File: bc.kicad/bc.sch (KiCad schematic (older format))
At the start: 19 parts, among them J1 Pin_Header_01x33_Male, J2 Capacitive Keyboard

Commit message: Experiment with keyboard backlighting
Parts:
- removed D1: LED_C1, bc:side_led, symbol Device:LED_Small
- removed D10: LED_A1_T, bc:side_led, symbol Device:LED_Small
- removed D11: LED_A1_B, bc:side_led, symbol Device:LED_Small
- removed D12: LED_A#1, bc:side_led, symbol Device:LED_Small
- removed D13: LED_B1_T, bc:side_led, symbol Device:LED_Small
- removed D14: LED_B1_B, bc:side_led, symbol Device:LED_Small
- removed D15: LED_C2_T, bc:side_led, symbol Device:LED_Small
- removed D16: LED_C2_B, bc:side_led, symbol Device:LED_Small
- removed D2: LED_C#1, bc:side_led, symbol Device:LED_Small
- removed D3: LED_D1, bc:side_led, symbol Device:LED_Small
- removed D4: LED_D#1, bc:side_led, symbol Device:LED_Small
- removed D5: LED_E1, bc:side_led, symbol Device:LED_Small
- removed D6: LED_F1, bc:side_led, symbol Device:LED_Small
- removed D7: LED_F#1, bc:side_led, symbol Device:LED_Small
- removed D8: LED_G1, bc:side_led, symbol Device:LED_Small
- removed D9: LED_G#1, bc:side_led, symbol Device:LED_Small
- removed J1: Pin_Header_01x33_Male, Connector_PinHeader_2.54mm:PinHeader_1x33_P2.54mm_Vertical_SMD_Pin1Left, symbol Connector:Conn_01x33_Male
- added BT?: CR2016, Battery:BatteryHolder_Keystone_3002_1x2032, symbol Device:Battery_Cell
- added C? (x6): 500nF, symbol Device:C
- added D? (x4): D_Schottky, symbol Device:D_Schottky
- added D? (x21): LED, symbol Device:LED
- added J?: Edge Connector, symbol Connector:Conn_01x08_Male
- added U?: STM32L052C8Tx, Package_QFP:LQFP-48_7x7mm_P0.5mm, symbol MCU_ST_STM32L0:STM32L052C8Tx
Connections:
- net labels added: BOOT0, DAC_OUT, GND, KEY_01_C1, KEY_02_C#1, KEY_03_D1, KEY_04_D#1, KEY_05_E1, KEY_06_F1, KEY_07_F#1, KEY_08_G1, KEY_09_G#1, KEY_10_A1, KEY_11_A#1, KEY_12_B1, KEY_13_C2, KEY_SAMP_C1, KEY_SAMP_C2, KEY_SAMP_C3, KEY_SAMP_C4, KEY_SAMP_C5, LED_C0, LED_C2, LED_C3, LED_R0, LED_R1, LED_R2, LED_R3, NRST, SWCLK, SWDIO, USART_RX, USART_TX, VDD
- net labels removed: ACT_SHLD, CAP_A#1, CAP_A1, CAP_B1, CAP_C#1, CAP_C1, CAP_C2, CAP_D#1, CAP_D1, CAP_E1, CAP_F#1, CAP_F1, CAP_G#1, CAP_G1, GNDD, LED_A#1, LED_A1_B, LED_A1_T, LED_B1_B, LED_B1_T, LED_C#1, LED_C2_B, LED_C2_T, LED_D#1, LED_D1, LED_E1, LED_F#1, LED_F1, LED_G#1, LED_G1, LED_GND, SPEAKER+, SPEAKER-
- wire segments 72 -> 146
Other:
- moved on the sheet: J2

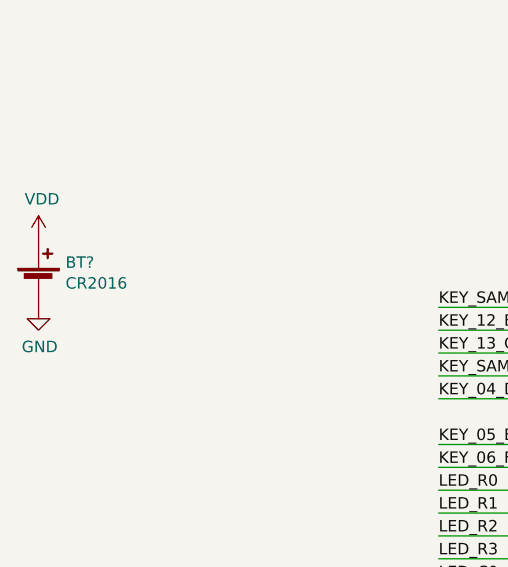
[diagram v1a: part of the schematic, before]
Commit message: Switch from CR2016 to CR2032
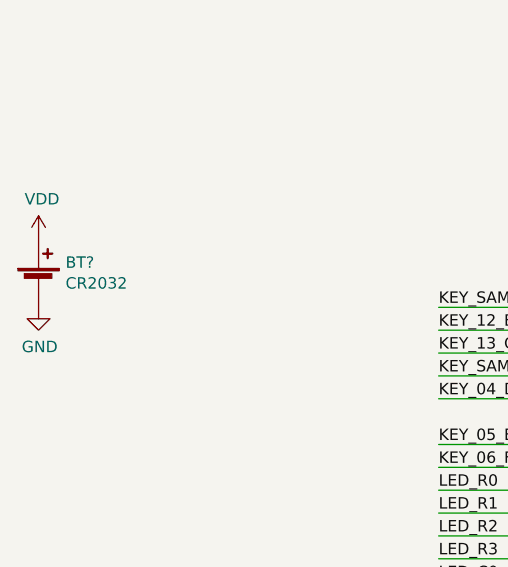
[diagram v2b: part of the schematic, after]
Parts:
- BT?: value CR2016 -> CR2032
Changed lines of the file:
@@
 P 1200 5450
 F 0 "BT?" H 1318 5546 50  0000 L CNN
-F 1 "CR2016" H 1318 5455 50  0000 L CNN
+F 1 "CR2032" H 1318 5455 50  0000 L CNN
 F 2 "Battery:BatteryHolder_Keystone_3002_1x2032" V 1200 5510 50  0001 C CNN
 F 3 "~" V 1200 5510 50  0001 C CNN

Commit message: Verify touch sensing design
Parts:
- removed J2: Capacitive Keyboard, bc:keyboard, symbol Connector:Conn_01x13_Female
- removed LS1: Speaker, bc:wire_pad_3x5mm_x2, symbol Device:Speaker
- added C? (x8): 500nF, symbol Device:C
- added C? (x12): 100nF, symbol Device:C
- added C? (x2): Capacitive_Keyboard, symbol bc:Capacitive_Keyboard
- added D? (x5): D_Schottky, symbol Device:D_Schottky
- added D? (x8): LED, symbol Device:LED
- added LS?: Transducer, symbol Device:Speaker_Crystal
- added Q?: PMV48XP, symbol Device:Q_PMOS_GSD
- added R? (x20): 10K, symbol Device:R
- added SW?: SW_Push, symbol Switch:SW_Push
- U?: symbol MCU_ST_STM32L0:STM32L052C8Tx -> bc:STM32L052C8Tx
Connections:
- net BOOT0: now also U?.44 (BOOT0), R?.2
- net GND: now also C?.1, C?.1, C?.1, C?.1, C?.1, C?.1, C?.1, C?.2, C?.2, C?.2, LS?.2, Q?.1 (G), R?.1, R?.1
- net KEY_01_C1: now also R?.1
- net KEY_02_C#1: now also R?.1
- net KEY_03_D1: now also R?.1
- net KEY_04_D#1: now also U?.16 (PA6), R?.1; no longer U?.40 (PB4)
- net KEY_05_E1: now also U?.17 (PA7), R?.1; no longer U?.42 (PB6)
- net KEY_06_F1: now also U?.19 (PB1), R?.1; no longer U?.43 (PB7)
- net KEY_07_F#1: now also U?.20 (PB2), R?.1; no longer U?.31 (PA10)
- net KEY_08_G1: now also U?.31 (PA10), R?.1; no longer U?.32 (PA11)
- net KEY_09_G#1: now also U?.32 (PA11), R?.1, R?.1; no longer U?.33 (PA12)
- net KEY_10_A1: now also U?.33 (PA12), R?.1, R?.1; no longer U?.16 (PA6)
- net KEY_11_A#1: now also U?.40 (PB4), R?.1, R?.1; no longer U?.17 (PA7)
- net KEY_12_B1: now also U?.42 (PB6), R?.1, R?.1; no longer U?.19 (PB1)
- net KEY_13_C2: now also U?.43 (PB7), R?.1, R?.1; no longer U?.20 (PB2)
- net KEY_SAMP_C1: now also C?.2
- net KEY_SAMP_C2: now also U?.15 (PA5), C?.2; no longer U?.39 (PB3)
- net KEY_SAMP_C3: now also U?.18 (PB0), C?.2; no longer U?.30 (PA9)
- net KEY_SAMP_C4: now also U?.30 (PA9), C?.2, C?.2; no longer U?.15 (PA5)
- net KEY_SAMP_C5: now also U?.39 (PB3), C?.2, C?.2; no longer U?.18 (PB0)
- net LED_C0: now also C?.1
- net LED_C1: now also D?.1 (K), D?.1 (K), D?.1 (K), D?.1 (K), D?.1 (K), D?.1 (K), D?.1 (K), D?.1 (K)
- net LED_R0: now also C?.1, C?.1
- net LED_R1: now also C?.1, C?.1
- net LED_R2: now also C?.1, C?.1
- net LED_R3: now also C?.1
- net NRST: now also U?.7 (NRST), C?.1
- net SWCLK: now also U?.37 (PA14)
- net SWDIO: now also U?.34 (PA13)
- net VDD: now also U?.1 (VDD), C?.1, C?.1, C?.1, C?.1, D?.2 (A), D?.2 (A), D?.2 (A), D?.2 (A), D?.2 (A), Q?.2 (S), SW?.1; no longer BT?.1 (+)
- net WKUP_MODE: now reaches U?.2 (PC13)
- net WKUP_MODE: now also R?.2, SW?.2
- net TRANSDUCER: now reaches U?.41 (PB5)
- net TRANSDUCER: now also LS?.1
- new net: BT?.1 (+), Q?.3 (D)
- new net: C?.2, C?.2, D?.1 (K), D?.2 (A), D?.2 (A) (x3)
- new net: C?.2, D?.1 (K), D?.2 (A) (x2)
- new net: C?.10 (10_A1), R?.2 (x2)
- new net: C?.11 (11_A#1), R?.2 (x2)
- new net: C?.12 (12_B1), R?.2 (x2)
- new net: C?.13 (13_C2), R?.2 (x2)
- new net: C?.9 (09_G#1), R?.2 (x2)
- new net: C?.1 (01_C1), R?.2
- new net: C?.2 (02_C#1), R?.2
- new net: C?.3 (03_D1), R?.2
- new net: C?.4 (04_D#1), R?.2
- new net: C?.5 (05_E1), R?.2
- new net: C?.6 (06_F1), R?.2
- new net: C?.7 (07_F#1), R?.2
- new net: C?.8 (08_G1), R?.2
- no-connect marks 0 -> 6
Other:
- note added: "1"
- note added: "2"
- note added: "3"
- note added: "4"
- note added: "5"
- note added: "CAP1"
- note added: "CAP2"
- note added: "CAP3"
- note added: "CAP4"
- note added: "CAP5"
- note added: "KEY01"
- note added: "KEY02"
- note added: "KEY03"
- note added: "KEY04"
- note added: "KEY05"
- note added: "KEY06"
- note added: "KEY07"
- note added: "KEY08"
- note added: "KEY09"
- note added: "KEY10"
- note added: "KEY11"
- note added: "KEY12"
- note added: "KEY13"
- note added: "PA11"
- note added: "PA12"
- note added: "PA9"
- note added: "PB10"
- note added: "PB11"
- note added: "PB12"
- note added: "PB13"
- note added: "PB3"
- note added: "PB4"
- note added: "PB6"
- note added: "PB7"
- note added: "PB8"
- note added: "PB9"
- note added: "TSC groups\n\n1: PA0-PA3\n2: PA5-PA7\n3: PB0-PB2\n4: PA9-PA12\n5: PB3, PB4, PB6, PB7"
- moved on the sheet: BT?, C?, D?, J?, U?

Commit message: Validate LED control circuit
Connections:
- net labels added: LED_R0_CLK, LED_R0_PWR, LED_R1_CLK, LED_R1_PWR, LED_R2_CLK, LED_R2_PWR, LED_R3_CLK, LED_R3_PWR
- net labels removed: DAC_OUT, LED_R0, LED_R1, LED_R2, LED_R3
- wire segments 242 -> 256
- no-connect marks 6 -> 3
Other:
- note added: "PA4"
- note added: "PA5"
- note added: "PA6"
- note added: "PA7"
- note added: "PA8"
- note removed: "PB13"
- moved on the sheet: C?, D?, R?

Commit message: Connect VDD to ADC
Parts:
- removed C? (x8): 500nF, symbol Device:C
- removed C?: Capacitive_Keyboard, symbol bc:Capacitive_Keyboard
- removed C? (x2): 100nF, symbol Device:C
- removed D? (x5): D_Schottky, symbol Device:D_Schottky
- removed D? (x8): LED, symbol Device:LED
- removed R? (x5): 10K, symbol Device:R
- added R2: 10K, symbol Device:R
- gave numbers to parts that had none: 63
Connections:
- net labels added: VDD_ADC
- wire segments 256 -> 202
- no-connect marks 3 -> 2
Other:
- note removed: "PA11"
- note removed: "PA12"
- note removed: "PA4"
- note removed: "PA5"
- note removed: "PA6"
- note removed: "PA7"
- note removed: "PA8"
- note removed: "PA9"
- note removed: "PB10"
- note removed: "PB11"
- note removed: "PB12"
- note removed: "PB3"
- note removed: "PB4"
- note removed: "PB6"
- note removed: "PB7"
- note removed: "PB8"
- note removed: "PB9"
- moved on the sheet: BT1, C10, C8, Q1

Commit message: Add bypassing to compensate for LED boosters
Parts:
- added C11, C12, C13, C14: 500nF, symbol Device:C
- renumbered C11 to C15, C12 to C16, C13 to C17, C14 to C18, C15 to C19, C16 to C20, C17 to C21
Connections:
- net GND: now also C11.2, C12.2, C13.2, C14.2
- net VDD: now also C11.1, C12.1, C13.1, C14.1
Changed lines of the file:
@@
 $EndComp
 $Comp
-L power:VDD #PWR014
+L power:VDD #PWR022
 U 1 1 5FD47C4E
 P 6100 3500
-F 0 "#PWR014" H 6100 3350 50  0001 C CNN
+F 0 "#PWR022" H 6100 3350 50  0001 C CNN
 F 1 "VDD" H 6115 3673 50  0000 C CNN
 F 2 "" H 6100 3500 50  0001 C CNN
@@
 $EndComp
 $Comp
-L power:GND #PWR015
+L power:GND #PWR023
 U 1 1 5FD4B605
 P 6100 3800
-F 0 "#PWR015" H 6100 3550 50  0001 C CNN
+F 0 "#PWR023" H 6100 3550 50  0001 C CNN
 F 1 "GND" H 6105 3627 50  0000 C CNN
 F 2 "" H 6100 3800 50  0001 C CNN
@@
 	6450 1550 6150 1550
 $Comp
-L power:GND #PWR019
+L power:GND #PWR027
 U 1 1 5FF011C9
 P 6850 1850
-F 0 "#PWR019" H 6850 1600 50  0001 C CNN
+F 0 "#PWR027" H 6850 1600 50  0001 C CNN
 F 1 "GND" H 6855 1677 50  0000 C CNN
 F 2 "" H 6850 1850 50  0001 C CNN
@@
 $EndComp
 $Comp
-L Device:C C11
+L Device:C C15
 U 1 1 5FD8985A
 P 6450 1700
-F 0 "C11" H 6565 1746 50  0000 L CNN
+F 0 "C15" H 6565 1746 50  0000 L CNN
 F 1 "100nF" H 6565 1655 50  0000 L CNN
 F 2 "" H 6488 1550 50  0001 C CNN
@@
 Connection ~ 6450 1550
 $Comp
-L power:GND #PWR017
+L power:GND #PWR025
 U 1 1 5FDD714C
 P 6450 1850
-F 0 "#PWR017" H 6450 1600 50  0001 C CNN
+F 0 "#PWR025" H 6450 1600 50  0001 C CNN
 F 1 "GND" H 6455 1677 50  0000 C CNN
 F 2 "" H 6450 1850 50  0001 C CNN
@@
 $EndComp
 $Comp
-L power:VDD #PWR018
+L power:VDD #PWR026
 U 1 1 5FEFF5F2
 P 6850 750
-F 0 "#PWR018" H 6850 600 50  0001 C CNN
+F 0 "#PWR026" H 6850 600 50  0001 C CNN
 F 1 "VDD" H 6865 923 50  0000 C CNN
 F 2 "" H 6850 750 50  0001 C CNN
@@
 NoConn ~ 2400 2100
 $Comp
-L power:GND #PWR016
+L power:GND #PWR024
 U 1 1 5FED77A2
 P 6250 650
-F 0 "#PWR016" H 6250 400 50  0001 C CNN
+F 0 "#PWR024" H 6250 400 50  0001 C CNN
 F 1 "GND" H 6255 477 50  0000 C CNN
 F 2 "" H 6250 650 50  0001 C CNN
@@
 CAP5
 $Comp
-L Device:C C12
+L Device:C C16
 U 1 1 602A0CFC
 P 8450 850
-F 0 "C12" V 8198 850 50  0000 C CNN
+F 0 "C16" V 8198 850 50  0000 C CNN
 F 1 "100nF" V 8289 850 50  0000 C CNN
 F 2 "" H 8488 700 50  0001 C CNN
@@
 	7750 850  8300 850
 $Comp
-L power:GND #PWR020
+L power:GND #PWR028
 U 1 1 602CDE2E
 P 8700 850
-F 0 "#PWR020" H 8700 600 50  0001 C CNN
+F 0 "#PWR028" H 8700 600 50  0001 C CNN
 F 1 "GND" H 8705 677 50  0000 C CNN
 F 2 "" H 8700 850 50  0001 C CNN
@@
 $EndComp
 $Comp
-L Device:C C13
+L Device:C C17
 U 1 1 602E6718
 P 8450 1250
-F 0 "C13" V 8198 1250 50  0000 C CNN
+F 0 "C17" V 8198 1250 50  0000 C CNN
 F 1 "100nF" V 8289 1250 50  0000 C CNN
 F 2 "" H 8488 1100 50  0001 C CNN
@@
 	7750 1250 8300 1250
 $Comp
-L power:GND #PWR021
+L power:GND #PWR029
 U 1 1 602E6720
 P 8700 1250
-F 0 "#PWR021" H 8700 1000 50  0001 C CNN
+F 0 "#PWR029" H 8700 1000 50  0001 C CNN
 F 1 "GND" H 8705 1077 50  0000 C CNN
 F 2 "" H 8700 1250 50  0001 C CNN
@@
 $EndComp
 $Comp
-L Device:C C14
+L Device:C C18
 U 1 1 602F0C05
 P 8450 1650
-F 0 "C14" V 8198 1650 50  0000 C CNN
+F 0 "C18" V 8198 1650 50  0000 C CNN
 F 1 "100nF" V 8289 1650 50  0000 C CNN
 F 2 "" H 8488 1500 50  0001 C CNN
@@
 	7750 1650 8300 1650
 $Comp
-L power:GND #PWR022
+L power:GND #PWR030
 U 1 1 602F0C0D
 P 8700 1650
-F 0 "#PWR022" H 8700 1400 50  0001 C CNN
+F 0 "#PWR030" H 8700 1400 50  0001 C CNN
 F 1 "GND" H 8705 1477 50  0000 C CNN
 F 2 "" H 8700 1650 50  0001 C CNN
@@
 $EndComp
 $Comp
-L Device:C C15
+L Device:C C19
 U 1 1 602FB737
 P 8450 2050
-F 0 "C15" V 8198 2050 50  0000 C CNN
+F 0 "C19" V 8198 2050 50  0000 C CNN
 F 1 "100nF" V 8289 2050 50  0000 C CNN
 F 2 "" H 8488 1900 50  0001 C CNN
@@
 	7750 2050 8300 2050
 $Comp
-L power:GND #PWR023
+L power:GND #PWR031
 U 1 1 602FB73F
 P 8700 2050
-F 0 "#PWR023" H 8700 1800 50  0001 C CNN
+F 0 "#PWR031" H 8700 1800 50  0001 C CNN
 F 1 "GND" H 8705 1877 50  0000 C CNN
 F 2 "" H 8700 2050 50  0001 C CNN
@@
 $EndComp
 $Comp
-L Device:C C16
+L Device:C C20
 U 1 1 60331281
 P 8450 2450
-F 0 "C16" V 8198 2450 50  0000 C CNN
+F 0 "C20" V 8198 2450 50  0000 C CNN
 F 1 "100nF" V 8289 2450 50  0000 C CNN
 F 2 "" H 8488 2300 50  0001 C CNN
@@
 	7750 2450 8300 2450
 $Comp
-L power:GND #PWR024
+L power:GND #PWR032
 U 1 1 60331289
 P 8700 2450
-F 0 "#PWR024" H 8700 2200 50  0001 C CNN
+F 0 "#PWR032" H 8700 2200 50  0001 C CNN
 F 1 "GND" H 8705 2277 50  0000 C CNN
 F 2 "" H 8700 2450 50  0001 C CNN
@@
 	8600 2450 8700 2450
 $Comp
-L bc:Capacitive_Keyboard C17
+L bc:Capacitive_Keyboard C21
 U 1 1 604A2F45
 P 10350 1800
-F 0 "C17" H 10650 3000 50  0000 L CNN
+F 0 "C21" H 10650 3000 50  0000 L CNN
 F 1 "Capacitive_Keyboard" H 10300 2900 50  0000 L CNN
 F 2 "" H 10350 1500 50  0001 C CNN
@@
 Text Label 6850 3500 2    50   ~ 0
 VDD_ADC
+$Comp
+L Device:C C11
+U 1 1 601E1C28
+P 4950 900
+F 0 "C11" H 5065 946 50  0000 L CNN
+F 1 "500nF" H 5065 855 50  0000 L CNN
+F 2 "" H 4988 750 50  0001 C CNN
+F 3 "~" H 4950 900 50  0001 C CNN
+	1    4950 900
+	1    0    0    -1
+$EndComp
+$Comp
+L Device:C C13
+U 1 1 601E1C2E
+P 5450 900
+F 0 "C13" H 5565 946 50  0000 L CNN
+F 1 "500nF" H 5565 855 50  0000 L CNN
+F 2 "" H 5488 750 50  0001 C CNN
+F 3 "~" H 5450 900 50  0001 C CNN
+	1    5450 900
+	1    0    0    -1
+$EndComp
+$Comp
+L Device:C C12
+U 1 1 601E1C34
+P 4950 1700
+F 0 "C12" H 5065 1746 50  0000 L CNN
+F 1 "500nF" H 5065 1655 50  0000 L CNN
+F 2 "" H 4988 1550 50  0001 C CNN
+F 3 "~" H 4950 1700 50  0001 C CNN
+	1    4950 1700
+	1    0    0    -1
+$EndComp
+$Comp
+L Device:C C14
+U 1 1 601E1C3A
+P 5450 1700
+F 0 "C14" H 5565 1746 50  0000 L CNN
+F 1 "500nF" H 5565 1655 50  0000 L CNN
+F 2 "" H 5488 1550 50  0001 C CNN
+F 3 "~" H 5450 1700 50  0001 C CNN
+	1    5450 1700
+	1    0    0    -1
+$EndComp
+$Comp
+L power:VDD #PWR014
+U 1 1 601E1C40
+P 4950 750
+F 0 "#PWR014" H 4950 600 50  0001 C CNN
+F 1 "VDD" H 4965 923 50  0000 C CNN
+F 2 "" H 4950 750 50  0001 C CNN
+F 3 "" H 4950 750 50  0001 C CNN
+	1    4950 750
+	1    0    0    -1
+$EndComp
+$Comp
+L power:VDD #PWR018
+U 1 1 601E1C46
+P 5450 750
+F 0 "#PWR018" H 5450 600 50  0001 C CNN
+F 1 "VDD" H 5465 923 50  0000 C CNN
+F 2 "" H 5450 750 50  0001 C CNN
+F 3 "" H 5450 750 50  0001 C CNN
+	1    5450 750
+	1    0    0    -1
+$EndComp
+$Comp
+L power:VDD #PWR016
+U 1 1 601E1C4C
+P 4950 1550
+F 0 "#PWR016" H 4950 1400 50  0001 C CNN
+F 1 "VDD" H 4965 1723 50  0000 C CNN
+F 2 "" H 4950 1550 50  0001 C CNN
+F 3 "" H 4950 1550 50  0001 C CNN
+	1    4950 1550
+	1    0    0    -1
+$EndComp
+$Comp
+L power:VDD #PWR020
+U 1 1 601E1C52
+P 5450 1550
+F 0 "#PWR020" H 5450 1400 50  0001 C CNN
+F 1 "VDD" H 5465 1723 50  0000 C CNN
+F 2 "" H 5450 1550 50  0001 C CNN
+F 3 "" H 5450 1550 50  0001 C CNN
+	1    5450 1550
+	1    0    0    -1
+$EndComp
+$Comp
+L power:GND #PWR019
+U 1 1 601E1C58
+P 5450 1050
+F 0 "#PWR019" H 5450 800 50  0001 C CNN
+F 1 "GND" H 5455 877 50  0000 C CNN
+F 2 "" H 5450 1050 50  0001 C CNN
+F 3 "" H 5450 1050 50  0001 C CNN
+	1    5450 1050
+	1    0    0    -1
+$EndComp
+$Comp
+L power:GND #PWR015
+U 1 1 601E1C5E
+P 4950 1050
+F 0 "#PWR015" H 4950 800 50  0001 C CNN
+F 1 "GND" H 4955 877 50  0000 C CNN
+F 2 "" H 4950 1050 50  0001 C CNN
+F 3 "" H 4950 1050 50  0001 C CNN
+	1    4950 1050
+	1    0    0    -1
+$EndComp
+$Comp
+L power:GND #PWR017
+U 1 1 601E1C64
+P 4950 1850
+F 0 "#PWR017" H 4950 1600 50  0001 C CNN
+F 1 "GND" H 4955 1677 50  0000 C CNN
+F 2 "" H 4950 1850 50  0001 C CNN
+F 3 "" H 4950 1850 50  0001 C CNN
+	1    4950 1850
+	1    0    0    -1
+$EndComp
+$Comp
+L power:GND #PWR021
+U 1 1 601E1C6A
+P 5450 1850
+F 0 "#PWR021" H 5450 1600 50  0001 C CNN
+F 1 "GND" H 5455 1677 50  0000 C CNN
+F 2 "" H 5450 1850 50  0001 C CNN
+F 3 "" H 5450 1850 50  0001 C CNN
+	1    5450 1850
+	1    0    0    -1
+$EndComp
 $EndSCHEMATC
